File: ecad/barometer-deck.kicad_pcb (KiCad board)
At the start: 2 copper layers, 25.2 x 27.3 mm, 3 parts, among them P1 CF_EXP_LEFT, P2 CF_EXP_RIGHT

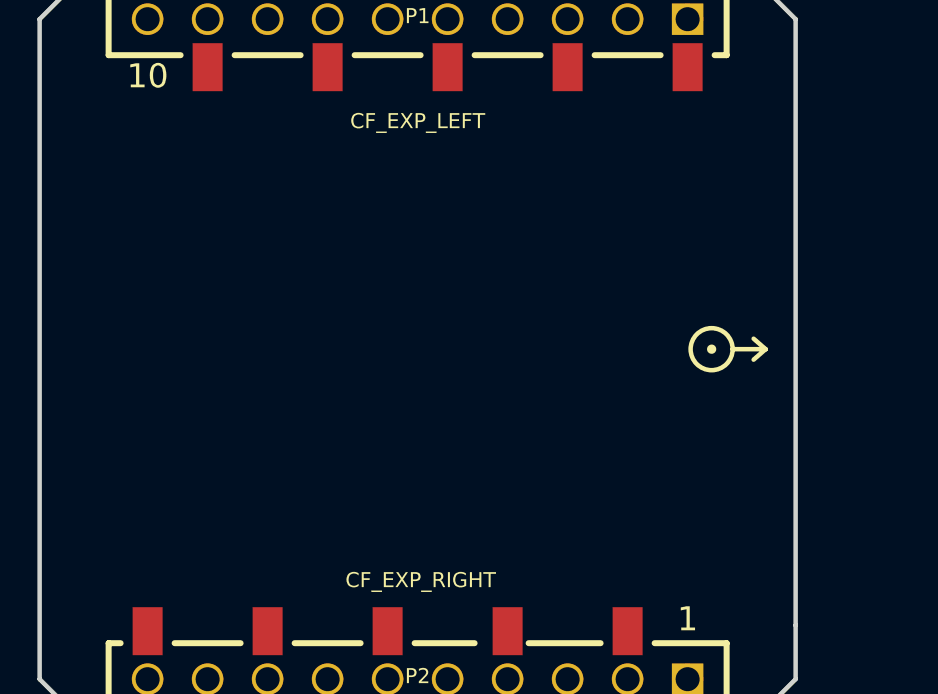
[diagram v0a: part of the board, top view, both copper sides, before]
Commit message: Initial schematics, power delviery module
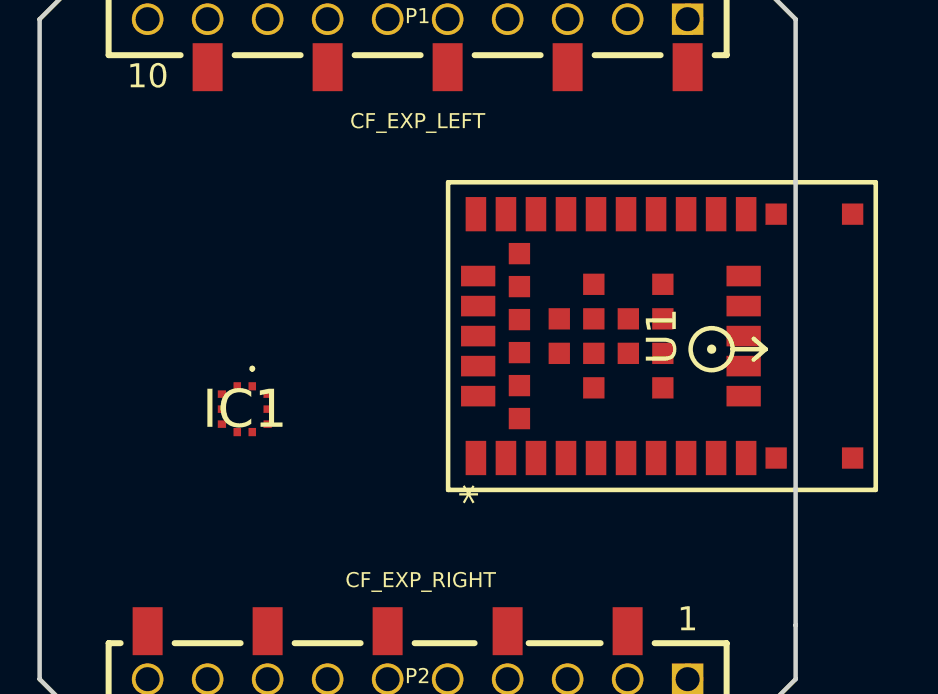
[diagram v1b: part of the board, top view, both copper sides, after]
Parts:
- added IC1: BMP390, BMP390:BMP390, F.Cu at (133.2, 99.0)
- added U1: NINA-W106-10B, NINA-W106_UBL:NINA-W106_UBL, F.Cu at (147.1, 96.6)
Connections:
- P1 pad 1: Net-(P1-Pad1) -> unconnected-(P1-VCC-Pad1)
- P1 pad 10: Net-(P1-Pad10) -> unconnected-(P1-GND-Pad10)
- P1 pad 2: Net-(P1-Pad2) -> unconnected-(P1-RX1-Pad2)
- P1 pad 3: Net-(P1-Pad3) -> unconnected-(P1-TX1-Pad3)
- P1 pad 4: Net-(P1-Pad4) -> unconnected-(P1-SDA-Pad4)
- P1 pad 5: Net-(P1-Pad5) -> unconnected-(P1-SCL-Pad5)
- P1 pad 6: Net-(P1-Pad6) -> unconnected-(P1-IO_1-Pad6)
- P1 pad 7: Net-(P1-Pad7) -> unconnected-(P1-IO_2-Pad7)
- P1 pad 8: Net-(P1-Pad8) -> unconnected-(P1-IO_3-Pad8)
- P1 pad 9: Net-(P1-Pad9) -> unconnected-(P1-IO_4-Pad9)
- P2 pad 1: Net-(P2-Pad1) -> unconnected-(P2-TX2-Pad1)
- P2 pad 10: Net-(P2-Pad10) -> unconnected-(P2-VUSB-Pad10)
- P2 pad 2: Net-(P2-Pad2) -> unconnected-(P2-RX2-Pad2)
- P2 pad 3: Net-(P2-Pad3) -> unconnected-(P2-SCK-Pad3)
- P2 pad 4: Net-(P2-Pad4) -> unconnected-(P2-MISO-Pad4)
- P2 pad 5: Net-(P2-Pad5) -> unconnected-(P2-MOSI-Pad5)
- P2 pad 6: Net-(P2-Pad6) -> unconnected-(P2-N_IO_1-Pad6)
- P2 pad 7: Net-(P2-Pad7) -> unconnected-(P2-WKUP-Pad7)
- P2 pad 8: Net-(P2-Pad8) -> unconnected-(P2-OW-Pad8)
- P2 pad 9: Net-(P2-Pad9) -> unconnected-(P2-VCOM-Pad9)

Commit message: jtag support
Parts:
- added C1: 1u, Capacitor_SMD:C_0402_1005Metric, F.Cu at (101.1, 96.2)
- added C2: 100n, Capacitor_SMD:C_0402_1005Metric, F.Cu at (101.1, 98.2)
- added C3: 10u, Capacitor_SMD:C_0402_1005Metric, F.Cu at (101.1, 100.1)
- added C4: 100n, Capacitor_SMD:C_0402_1005Metric, F.Cu at (101.1, 102.1)
- added C5: 100n, Capacitor_SMD:C_0402_1005Metric, F.Cu at (101.1, 104.1)
- added C6: 100n, Capacitor_SMD:C_0402_1005Metric, F.Cu at (101.1, 106.1)
- added C7: 100n, Capacitor_SMD:C_0402_1005Metric, F.Cu at (101.1, 108.0)
- added C8: 100n, Capacitor_SMD:C_0402_1005Metric, F.Cu at (101.1, 110.0)
- added D1: LED, LED_SMD:LED_0603_1608Metric, F.Cu at (107.5, 105.7)
- added D2: LED, LED_SMD:LED_0603_1608Metric, F.Cu at (107.5, 108.3)
- added IC1: MIC5353-3.3YMT-TR, MIC5353-3_3YMT-TR:SON50P160X160X60-7N-D, F.Cu at (111.5, 110.8)
- added R1: 4.7k, Resistor_SMD:R_0402_1005Metric, F.Cu at (104.0, 105.4)
- added R2: 4.7k, Resistor_SMD:R_0402_1005Metric, F.Cu at (104.0, 107.4)
- added R3: 10k, Resistor_SMD:R_0402_1005Metric, F.Cu at (104.0, 109.4)
- added R4: 1k, Resistor_SMD:R_0402_1005Metric, F.Cu at (104.0, 111.4)
- added R5: 1k, Resistor_SMD:R_0402_1005Metric, F.Cu at (104.0, 113.4)
- added TP1: TestPoint, Connector_PinHeader_2.54mm:PinHeader_1x01_P2.54mm_Vertical, F.Cu at (104.9, 97.5)
- added TP2: TestPoint, Connector_PinHeader_2.54mm:PinHeader_1x01_P2.54mm_Vertical, F.Cu at (104.9, 102.1)
- added TP3: TestPoint, Connector_PinHeader_2.54mm:PinHeader_1x01_P2.54mm_Vertical, F.Cu at (109.5, 97.5)
- added TP4: TestPoint, Connector_PinHeader_2.54mm:PinHeader_1x01_P2.54mm_Vertical, F.Cu at (109.5, 102.1)
- added TP5: TestPoint, Connector_PinHeader_2.54mm:PinHeader_1x01_P2.54mm_Vertical, F.Cu at (114.0, 97.5)
- added TP6: TestPoint, Connector_PinHeader_2.54mm:PinHeader_1x01_P2.54mm_Vertical, F.Cu at (114.0, 102.1)
- added U2: DS2431, Package_TO_SOT_SMD:SOT-23-3, F.Cu at (112.1, 106.6)
- P1, P2: footprint connectors:BF090-10-X-B2 -> Connector_PinSocket_2.00mm:PinSocket_1x10_P2.00mm_Vertical
- moved P1 9.28 mm to (148.3, 85.3), turned to -90 degrees
- moved P2 8.81 mm to (147.8, 109.0), turned to -90 degrees
- moved IC2 3.40 mm to (130.0, 100.0)
- moved U1 1.12 mm to (148.1, 96.1)
- renumbered IC1 to IC2
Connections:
- IC2 pad 1: unconnected-(IC1-VDDIO-Pad1) -> +3.3V
- IC2 pad 10: unconnected-(IC1-VDD-Pad10) -> +3.3V
- IC2 pad 2: unconnected-(IC1-SCK-Pad2) -> SCK
- IC2 pad 3: unconnected-(IC1-VSS_1-Pad3) -> GND
- IC2 pad 4: unconnected-(IC1-SDI-Pad4) -> SDA
- IC2 pad 5: unconnected-(IC1-SDO-Pad5) -> +3.3V
- IC2 pad 6: unconnected-(IC1-CSB-Pad6) -> +3.3V
- IC2 pad 8: unconnected-(IC1-VSS_2-Pad8) -> GND
- IC2 pad 9: unconnected-(IC1-VSS_3-Pad9) -> GND
- P1 pad 10: unconnected-(P1-GND-Pad10) -> GND
- P2 pad 8: unconnected-(P2-OW-Pad8) -> OW
- P2 pad 9: unconnected-(P2-VCOM-Pad9) -> VCOM
- U1 pad 10: unconnected-(U1-VCC-Pad10) -> +3.3V
- U1 pad 12: unconnected-(U1-GND-Pad12) -> GND
- U1 pad 14: unconnected-(U1-GND-Pad14) -> GND
- U1 pad 19: unconnected-(U1-RESET_N-Pad19) -> RST
- U1 pad 21: unconnected-(U1-GPIO_21/UART_CTS/RMII_TXD0/SPI_V_MISO-Pad21) -> SDA
- U1 pad 22: unconnected-(U1-GPIO_22/UART_TXD-Pad22) -> TXD
- U1 pad 23: unconnected-(U1-GPIO_23/UART_RXD-Pad23) -> RXD
- U1 pad 24: unconnected-(U1-GPIO_24/RMII_MDIO-Pad24) -> SCK
- U1 pad 26: unconnected-(U1-GND-Pad26) -> GND
- U1 pad 27: unconnected-(U1-GPIO_27/RMII_CLK/SYS_BOOT-Pad27) -> BOOT
- U1 pad 30: unconnected-(U1-GND-Pad30) -> GND
- U1 pad 37: unconnected-(U1-GND-Pad37) -> GND
- U1 pad 38: unconnected-(U1-GND-Pad38) -> GND
- U1 pad 39: unconnected-(U1-GND-Pad39) -> GND
- U1 pad 40: unconnected-(U1-GND-Pad40) -> GND
- U1 pad 41: unconnected-(U1-GND-Pad41) -> GND
- U1 pad 42: unconnected-(U1-GND-Pad42) -> GND
- U1 pad 43: unconnected-(U1-GND-Pad43) -> GND
- U1 pad 44: unconnected-(U1-GND-Pad44) -> GND
- U1 pad 45: unconnected-(U1-GND-Pad45) -> GND
- U1 pad 46: unconnected-(U1-GND-Pad46) -> GND
- U1 pad 47: unconnected-(U1-GND-Pad47) -> GND
- U1 pad 48: unconnected-(U1-GND-Pad48) -> GND
- U1 pad 49: unconnected-(U1-GND-Pad49) -> GND
- U1 pad 5: unconnected-(U1-GPIO_5-Pad5) -> WIFI_LED
- U1 pad 50: unconnected-(U1-GND-Pad50) -> GND
- U1 pad 51: unconnected-(U1-GND-Pad51) -> GND
- U1 pad 52: unconnected-(U1-GND-Pad52) -> GND
- U1 pad 6: unconnected-(U1-GND-Pad6) -> GND
- U1 pad 9: unconnected-(U1-VCC_IO-Pad9) -> +3.3V

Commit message: layout done
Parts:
- removed C8: 100n, Capacitor_SMD:C_0402_1005Metric
- removed TP1, TP2, TP3, TP4, TP5, TP6: TestPoint, Connector_PinHeader_2.54mm:PinHeader_1x01_P2.54mm_Vertical
- added J1: JTAG_EDGE, Connector_PinHeader_1.27mm:PinHeader_2x05_P1.27mm_Horizontal, F.Cu at (147.5, 101.3)
- added R6: 1k, Resistor_SMD:R_0402_1005Metric, F.Cu at (129.8, 97.0)
- R4: value 1k -> 330
- moved C6 53.2 mm to (150.8, 86.8)
- moved C7 46.7 mm to (147.0, 99.0)
- moved R4 37.0 mm to (140.5, 105.3), turned to 180 degrees
- moved R3 36.9 mm to (140.5, 103.8)
- moved C3 35.9 mm to (136.8, 105.0), turned to -90 degrees
- moved C5 35.8 mm to (135.3, 93.3)
- moved R2 34.9 mm to (135.3, 91.8)
- moved C2 34.7 mm to (135.8, 101.0)
- moved C1 34.7 mm to (134.8, 104.8)
- moved C4 32.6 mm to (131.5, 90.3), turned to 180 degrees
- moved R5 32.4 mm to (132.0, 97.0), turned to -90 degrees
- moved R1 32.0 mm to (131.5, 89.0), turned to 180 degrees
- moved IC1 25.6 mm to (135.8, 102.8)
- moved D1 25.1 mm to (132.0, 100.3), turned to 90 degrees
- moved D2 23.6 mm to (129.8, 100.3), turned to 90 degrees
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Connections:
- C6 pad 1: RST -> NINA_NRST
- P1 pad 2: unconnected-(P1-RX1-Pad2) -> RXD
- P1 pad 3: unconnected-(P1-TX1-Pad3) -> TXD
- P1 pad 4: unconnected-(P1-SDA-Pad4) -> SDA
- P1 pad 5: unconnected-(P1-SCL-Pad5) -> SCK
- R3 pad 2: RST -> NINA_NRST
- R4 pad 1: +3.3V -> Net-(J1-Pin_10)
- R4 pad 2: Net-(D1-A) -> NINA_NRST
- R5 pad 1: WIFI_LED -> +3.3V
- R5 pad 2: Net-(D2-A) -> Net-(D1-A)
- U1 pad 19: RST -> NINA_NRST
- U1 pad 27: BOOT -> unconnected-(U1-GPIO_27/RMII_CLK/SYS_BOOT-Pad27)
- U1 pad 29: unconnected-(U1-GPIO_29/SPI_V_CLK-Pad29) -> WIFI_LED
- U1 pad 31: unconnected-(U1-JTAG_TMS/GPIO_31-Pad31) -> NINA_JTAG_TMS
- U1 pad 32: unconnected-(U1-JTAG_TDO/GPIO_32-Pad32) -> NINA_JTAG_TDO
- U1 pad 35: unconnected-(U1-JTAG_TCK/GPIO_35-Pad35) -> NINA_JTAG_TCK
- U1 pad 36: unconnected-(U1-JTAG_TDI/GPIO_36-Pad36) -> NINA_JTAG_TDI
- U1 pad 5: WIFI_LED -> unconnected-(U1-GPIO_5-Pad5)
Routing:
- net +3.3V: track 0.00 -> 48.3 mm
- net NINA_NRST: track 0.00 -> 25.6 mm, vias 0 -> 2
- net NINA_JTAG_TDI: track 0.00 -> 24.9 mm, vias 0 -> 1
- net SDA: track 0.00 -> 21.8 mm, vias 0 -> 1
- net NINA_JTAG_TDO: track 0.00 -> 17.4 mm, vias 0 -> 1
- net NINA_JTAG_TCK: track 0.00 -> 16.8 mm, vias 0 -> 1
- net SCK: track 0.00 -> 14.9 mm, vias 0 -> 2
- net NINA_JTAG_TMS: track 0.00 -> 12.4 mm, vias 0 -> 2
- net WIFI_LED: track 0.00 -> 9.94 mm, vias 0 -> 2
- net Net-(J1-Pin_10): track 0.00 -> 8.98 mm
- net RXD: track 0.00 -> 8.49 mm, vias 0 -> 2
- net VCOM: track 0.00 -> 7.62 mm, vias 0 -> 1
- net TXD: track 0.00 -> 6.08 mm, vias 0 -> 1
- net GND: track 0.00 -> 4.58 mm, vias 0 -> 7
- net OW: track 0.00 -> 4.41 mm
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- added copper zone on B.Cu, net GND
- added copper zone on F.Cu, net GND
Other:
- board text removed: "uUSB TOP"

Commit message: layout update:
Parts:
- moved C7 0.50 mm to (146.5, 99.0)
- moved C6 0.08 mm to (150.7, 86.8)
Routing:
- net NINA_NRST: track 25.6 -> 40.2 mm, vias 2 -> 0
- net VCOM: track 7.62 -> 8.20 mm

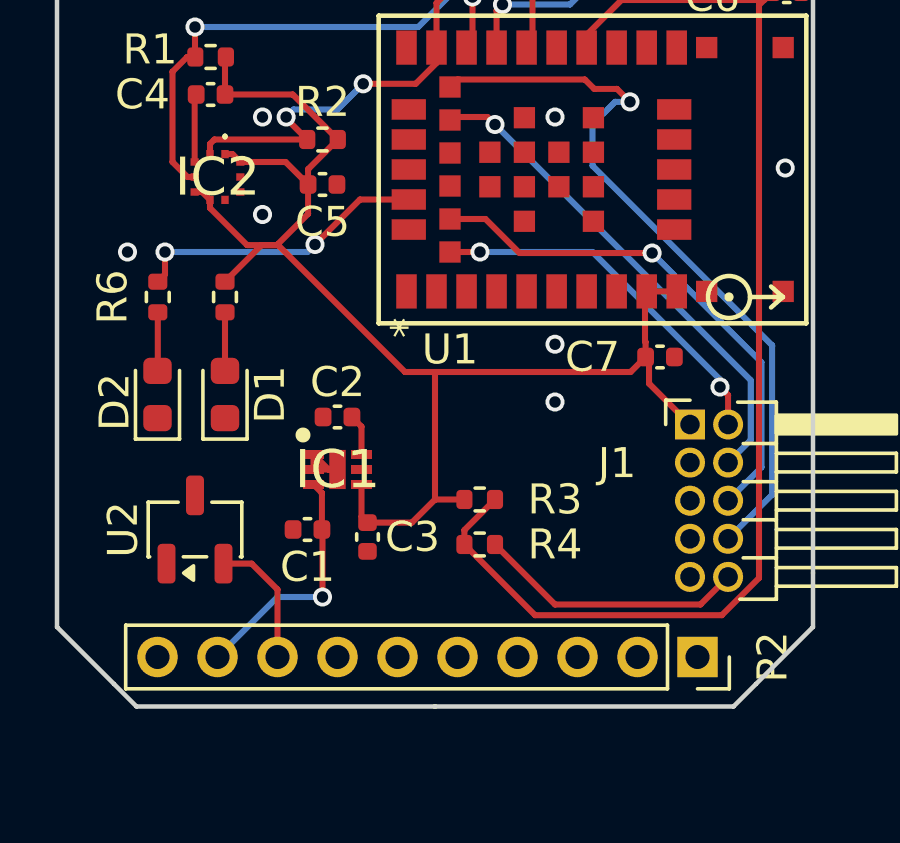
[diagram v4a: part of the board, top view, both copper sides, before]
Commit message: added thermal relief, thicken lines
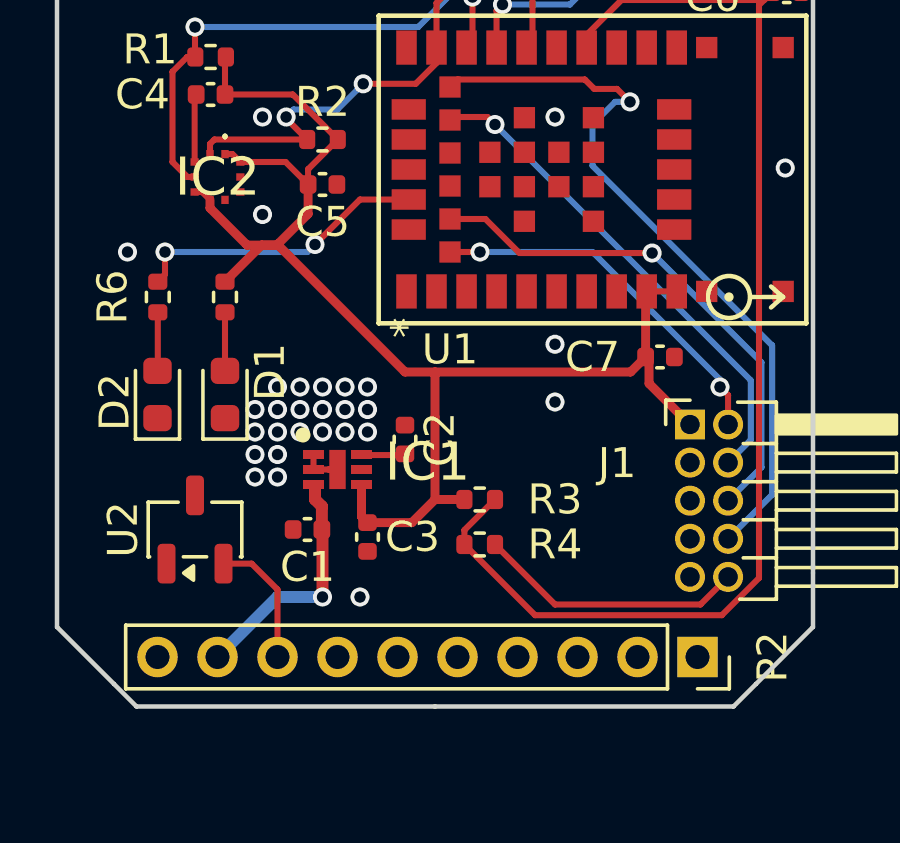
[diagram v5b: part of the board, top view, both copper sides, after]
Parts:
- moved C2 2.37 mm to (138.0, 101.8), turned to -90 degrees
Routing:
- net GND: track 4.58 -> 3.87 mm, vias 7 -> 29
